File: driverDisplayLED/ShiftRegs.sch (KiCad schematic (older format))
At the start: 8 parts, among them U5 74HC595, U6 74HC595, U7 74HC595, U8 74HC595

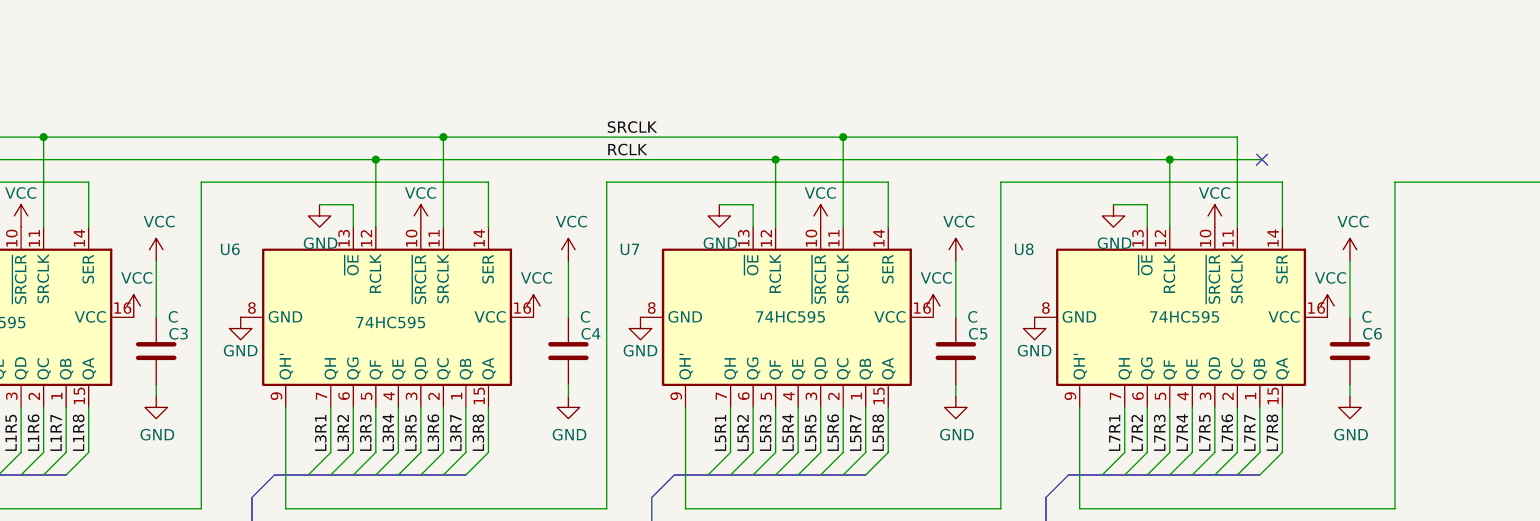
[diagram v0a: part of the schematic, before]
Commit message: Agrego codigos de catalogo, documentación, y linkeo del borrador del PCB
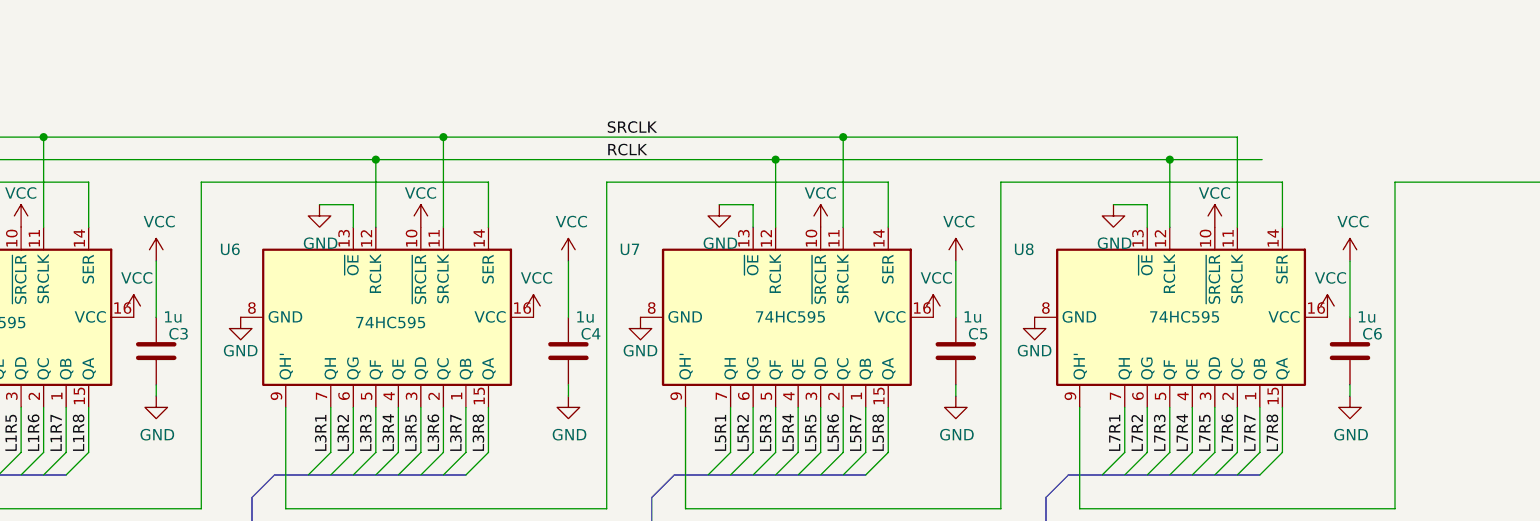
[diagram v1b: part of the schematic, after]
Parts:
- C3, C4, C5, C6: value C -> 1u
- U5, U6, U7, U8: CodigoCatalogo (none) -> 74HC595DR2GOSTR-ND - Tape & Reel (TR)
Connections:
- no-connect marks 2 -> 1
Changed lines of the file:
@@
 F 2 "Package_SO:SO-16_5.3x10.2mm_P1.27mm" H 6575 3300 50  0001 C CNN
 F 3 "http://www.ti.com/lit/ds/symlink/sn74hc595.pdf" H 6575 3300 50  0001 C CNN
+F 4 "74HC595DR2GOSTR-ND - Tape & Reel (TR)" V 6575 3300 50  0001 C CNN "CodigoCatalogo"
 	1    6575 3300
 	0    1    1    0
@@
 F 2 "Package_SO:SO-16_5.3x10.2mm_P1.27mm" H 4800 3300 50  0001 C CNN
 F 3 "http://www.ti.com/lit/ds/symlink/sn74hc595.pdf" H 4800 3300 50  0001 C CNN
+F 4 "74HC595DR2GOSTR-ND - Tape & Reel (TR)" V 4800 3300 50  0001 C CNN "CodigoCatalogo"
 	1    4800 3300
 	0    1    1    0
@@
 AR Path="/5FD444D5/601B149A" Ref="C3"  Part="1"
 F 0 "C3" H 3625 3375 50  0000 C CNN
-F 1 "C" H 3650 3300 50  0000 C CNN
+F 1 "1u" H 3650 3300 50  0000 C CNN
 F 2 "Capacitor_SMD:C_0201_0603Metric" H 3763 3300 50  0001 C CNN
 F 3 "~" H 3725 3450 50  0001 C CNN
@@
 F 2 "Package_SO:SO-16_5.3x10.2mm_P1.27mm" H 3025 3300 50  0001 C CNN
 F 3 "http://www.ti.com/lit/ds/symlink/sn74hc595.pdf" H 3025 3300 50  0001 C CNN
+F 4 "74HC595DR2GOSTR-ND - Tape & Reel (TR)" V 3025 3300 50  0001 C CNN "CodigoCatalogo"
 	1    3025 3300
 	0    1    1    0
@@
 AR Path="/5FD444D5/601B14CF" Ref="C4"  Part="1"
 F 0 "C4" H 5455 3375 50  0000 C CNN
-F 1 "C" H 5480 3300 50  0000 C CNN
+F 1 "1u" H 5480 3300 50  0000 C CNN
 F 2 "Capacitor_SMD:C_0201_0603Metric" H 5593 3300 50  0001 C CNN
 F 3 "~" H 5555 3450 50  0001 C CNN
@@
 AR Path="/5FD444D5/601B14E5" Ref="C5"  Part="1"
 F 0 "C5" H 7175 3375 50  0000 C CNN
-F 1 "C" H 7200 3300 50  0000 C CNN
+F 1 "1u" H 7200 3300 50  0000 C CNN
 F 2 "Capacitor_SMD:C_0201_0603Metric" H 7313 3300 50  0001 C CNN
 F 3 "~" H 7275 3450 50  0001 C CNN
@@
 AR Path="/5FD444D5/601B14FB" Ref="C6"  Part="1"
 F 0 "C6" H 8925 3375 50  0000 C CNN
-F 1 "C" H 8950 3300 50  0000 C CNN
+F 1 "1u" H 8950 3300 50  0000 C CNN
 F 2 "Capacitor_SMD:C_0201_0603Metric" H 9063 3300 50  0001 C CNN
 F 3 "~" H 9025 3450 50  0001 C CNN
@@
 F 2 "Package_SO:SO-16_5.3x10.2mm_P1.27mm" H 8325 3300 50  0001 C CNN
 F 3 "http://www.ti.com/lit/ds/symlink/sn74hc595.pdf" H 8325 3300 50  0001 C CNN
+F 4 "74HC595DR2GOSTR-ND - Tape & Reel (TR)" V 8325 3300 50  0001 C CNN "CodigoCatalogo"
 	1    8325 3300
 	0    1    1    0
@@
 	8225 2600 8635 2600
 Connection ~ 8225 2600
-NoConn ~ 8635 2600
 Wire Bus Line
 	7775 4000 8625 4000

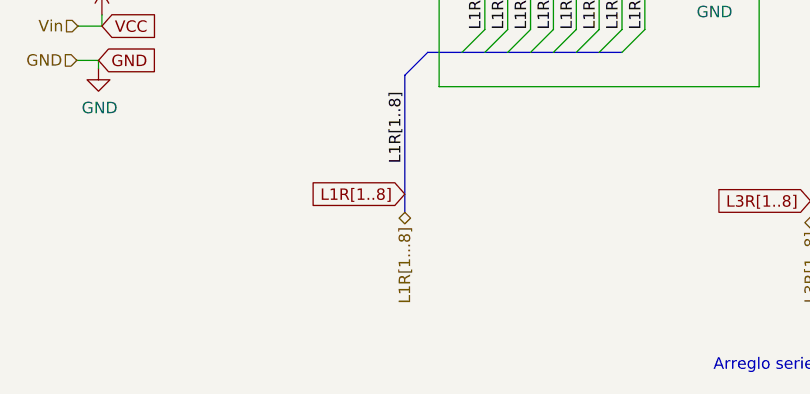
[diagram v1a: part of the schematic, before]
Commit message: Agrego nuevo proyecto: Modulo Infrarrojo TxRx
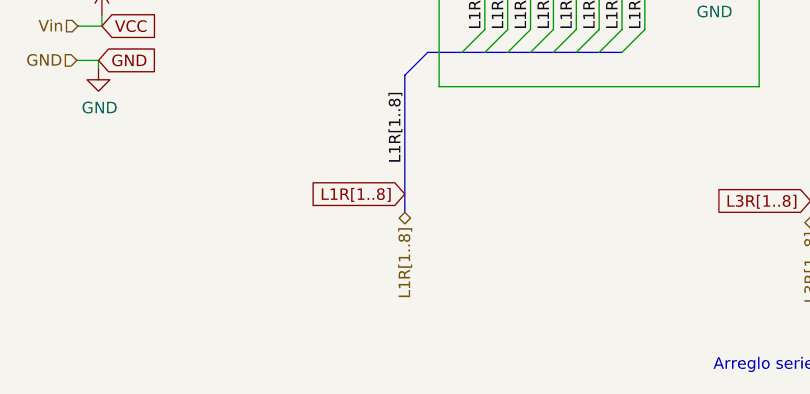
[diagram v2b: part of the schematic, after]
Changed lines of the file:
@@
 L1R[1..8]
 Text HLabel 2375 4700 3    50   BiDi ~ 0
-L1R[1...8]
+L1R[1..8]
 Text GLabel 4150 4650 0    50   Input ~ 0
 L3R[1..8]
